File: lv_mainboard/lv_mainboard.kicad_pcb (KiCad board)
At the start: 2 copper layers, 140 x 250 mm, 80 parts, among them J1 Conn_01x02, J10 PWR, J11 Conn_02x05_Counter_Clockwise, J12 Conn_01x04, J13 Conn_02x10_Odd_Even, J14 Conn_01x04, J15 PWR, J16 Conn_01x04, J17 Conn_01x04, J18 Conn_01x02, J19 PWR, J2 Conn_02x10_Odd_Even, J3 Conn_01x03, J4 Conn_01x04, J5 Conn_01x05, J6 Conn_02x10_Odd_Even, J7 Conn_02x10_Odd_Even, J8 Conn_01x04, J9 DE9_Plug_MountingHoles, U1 AP2204K-ADJ, U2 AP2204K-ADJ, U3 AP2204K-ADJ

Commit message: v2025.8
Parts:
- removed C1, C3: 1u, Resistor_SMD:R_0603_1608Metric
- removed C2, C4: 10u, Resistor_SMD:R_0805_2012Metric
- removed C5: 1u, Capacitor_SMD:C_0603_1608Metric_Pad1.08x0.95mm_HandSolder
- removed C6: 10u, Capacitor_SMD:C_0805_2012Metric_Pad1.18x1.45mm_HandSolder
- removed the J12 at (262.0, 311.0)
- removed the J12 at (262.0, 301.5)
- removed the J14 at (280.0, 311.0)
- removed the J14 at (280.0, 301.5)
- removed the J16 at (244.0, 301.5)
- removed the J16 at (244.0, 311.0)
- removed J17: Conn_01x04, Connector_JST:JST_XH_B4B-XH-A_1x04_P2.50mm_Vertical
- removed R3, R5, R7: 100k, Resistor_SMD:R_0603_1608Metric
- removed R4: 301k, Resistor_SMD:R_0603_1608Metric
- removed R6: 165k, Resistor_SMD:R_0603_1608Metric
- removed R8: 866k, Resistor_SMD:R_0603_1608Metric
- removed TP1, TP2, TP3: TestPoint, TestPoint:TestPoint_THTPad_D1.5mm_Drill0.7mm
- removed U1, U2, U3: AP2204K-ADJ, Package_TO_SOT_SMD:SOT-23-5
- removed kibuzzard-682D880A: G***, kibuzzard-682D880A
- removed kibuzzard-682D8819: G***, kibuzzard-682D8819
- removed kibuzzard-682D8830: G***, kibuzzard-682D8830
- removed kibuzzard-682D8907: G***, kibuzzard-682D8907
- removed kibuzzard-682D8919: G***, kibuzzard-682D8919
- removed kibuzzard-682D8927: G***, kibuzzard-682D8927
- removed kibuzzard-682D8AF9: G***, kibuzzard-682D8AF9
- removed kibuzzard-682D8B11: G***, kibuzzard-682D8B11
- removed kibuzzard-682D8B7A: G***, kibuzzard-682D8B7A
- removed kibuzzard-682D8C28: G***, kibuzzard-682D8C28
- removed kibuzzard-682D8E18: G***, kibuzzard-682D8E18
- added J12: Conn_01x04, Connector_JST:JST_XH_B4B-XH-A_1x04_P2.50mm_Vertical, F.Cu at (302.4, 227.4)
- added J14: Conn_01x04, Connector_JST:JST_XH_B4B-XH-A_1x04_P2.50mm_Vertical, F.Cu at (302.3, 244.6)
- added J16: Conn_01x04, Connector_JST:JST_XH_B4B-XH-A_1x04_P2.50mm_Vertical, F.Cu at (302.4, 261.5)
- added J20: Conn_01x02, Connector_JST:JST_XH_B2B-XH-A_1x02_P2.50mm_Vertical, F.Cu at (301.0, 154.5)
- added J21: Conn_01x02, Connector_JST:JST_XH_B2B-XH-A_1x02_P2.50mm_Vertical, F.Cu at (176.0, 202.5)
- added J22: Conn_01x02, Connector_JST:JST_XH_B2B-XH-A_1x02_P2.50mm_Vertical, F.Cu at (290.0, 154.5)
- added J23: Conn_01x03, Connector_JST:JST_XH_B3B-XH-A_1x03_P2.50mm_Vertical, F.Cu at (254.5, 74.5)
- added J24: PWR, Connector_AMASS:AMASS_XT60-M_1x02_P7.20mm_Vertical, F.Cu at (184.5, 89.0)
- added J25: Conn_01x04, Connector_JST:JST_XH_B4B-XH-A_1x04_P2.50mm_Vertical, F.Cu at (291.0, 227.5)
- added J26: Conn_01x04, Connector_JST:JST_XH_B4B-XH-A_1x04_P2.50mm_Vertical, F.Cu at (291.5, 244.7)
- added J27: Conn_01x04, Connector_JST:JST_XH_B4B-XH-A_1x04_P2.50mm_Vertical, F.Cu at (291.5, 261.6)
- J9: value DE9_Plug_MountingHoles -> PWR; footprint Connector_Dsub:DSUB-9_Female_Horizontal_P2.77x2.84mm_EdgePinOffset7.70mm_Housed_MountingHolesOffset9.12mm -> Connector_AMASS:AMASS_XT60-M_1x02_P7.20mm_Vertical
- R1, R2: moved to F.Cu
- moved J18 180.8 mm to (301.0, 167.0), turned to -90 degrees
- moved J4 166.1 mm to (301.5, 180.0)
- moved J8 138.6 mm to (302.0, 210.0)
- moved J9 128.1 mm to (184.6, 100.0), turned to 180 degrees
- moved J1 125.2 mm to (301.5, 196.1)
- moved H21 95.8 mm to (281.4, 168.3)
- moved H22 95.8 mm to (258.4, 168.3)
- moved H23 95.8 mm to (258.4, 211.3)
- moved H24 95.8 mm to (281.4, 211.3)
- moved J2 95.8 mm to (258.2, 201.2)
- moved G*** 75.2 mm to (344.2, 278.5)
- moved G*** 75.2 mm to (344.0, 269.0)
- moved G*** 75.2 mm to (344.0, 253.0)
- moved J5 70.6 mm to (237.5, 74.5), turned to 0 degrees
- moved J13 56.9 mm to (256.7, 126.9)
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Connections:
- J11 pad 3: P4_RGB -> P4_HVbox
- J2 pad 2: SW_signal -> SW_Fault
- J3 pad 2: FAN_PWR -> PUMP_PWR
- J3 pad 3: PUMP_PWR -> FAN_PWR
- J7 pad 11: unconnected-(J7-Pin_11-Pad11) -> GND
- J7 pad 13: unconnected-(J7-Pin_13-Pad13) -> GND
- J7 pad 15: unconnected-(J7-Pin_15-Pad15) -> GND
- J7 pad 17: unconnected-(J7-Pin_17-Pad17) -> GND
- J7 pad 5: unconnected-(J7-Pin_5-Pad5) -> GND
- J7 pad 7: unconnected-(J7-Pin_7-Pad7) -> GND
- J7 pad 9: unconnected-(J7-Pin_9-Pad9) -> GND
- J9 pad 1: BSE_L_init -> P4_HVbox
- J9 pad 2: CAN- -> GND
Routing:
- net GND: track 9.35 -> 416.4 mm, vias 2 -> 825
- net +3V3: track 321.5 -> 0.00 mm, vias 2 -> 0
- net +24V: track 0.00 -> 205.9 mm
- net P5_MCU: track 298.7 -> 109.4 mm
- net P7_ACC: track 340.4 -> 161.8 mm, vias 0 -> 1
- net current_init: track 16.1 -> 124.9 mm, vias 0 -> 2
- net BMS_RST: track 32.9 -> 115.6 mm
- net SW_Fault: track 0.00 -> 82.2 mm, vias 0 -> 1
- net BSPD_LED: track 32.3 -> 107.1 mm
- net BSPD_RST: track 31.2 -> 104.3 mm
- net PUMP_PWR: track 28.7 -> 94.6 mm, vias 0 -> 1
- net SDC_OUT: track 89.1 -> 25.2 mm
- net BMS_LED: track 30.8 -> 94.4 mm
- net FAN_PWR: track 28.7 -> 91.3 mm, vias 0 -> 1
- net P2_BSPD: track 143.2 -> 80.8 mm
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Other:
- board size 140 x 250 mm -> 140 x 220 mm
- board text removed: "GND LED RST VDD"
- board text removed: "GND TASL BMS_F IMD_F"
- board text removed: "GND TASL TSSI 24V"
- board text removed: "GND U1 T1 P1 U2"
- board text removed: "GND pump fan"
- board text removed: "PWM"
- board text removed: "current_in"
- board text removed: "from ACC Box"
- board text removed: "from HV Box"
- board text removed: "to ACC Box"
- board text removed: "to Mainhoop Light"

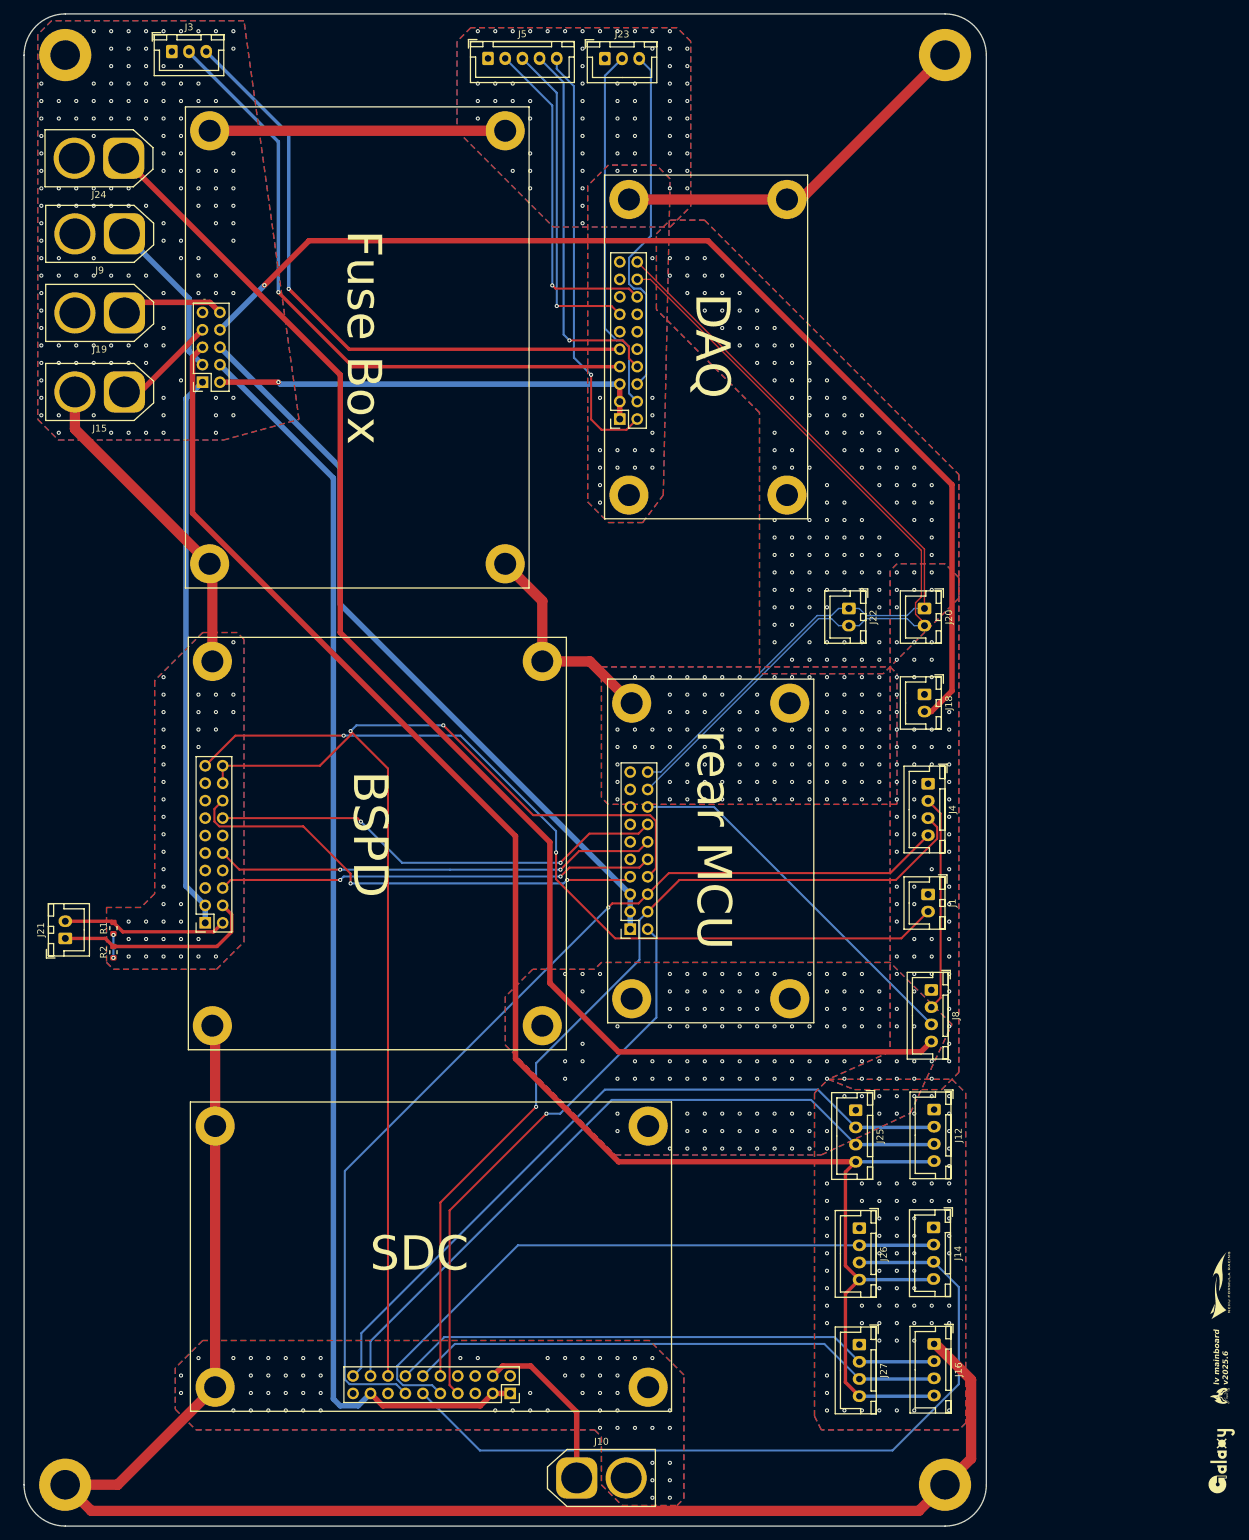
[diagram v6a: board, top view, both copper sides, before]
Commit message: v2025.8 but need to add another DAQ
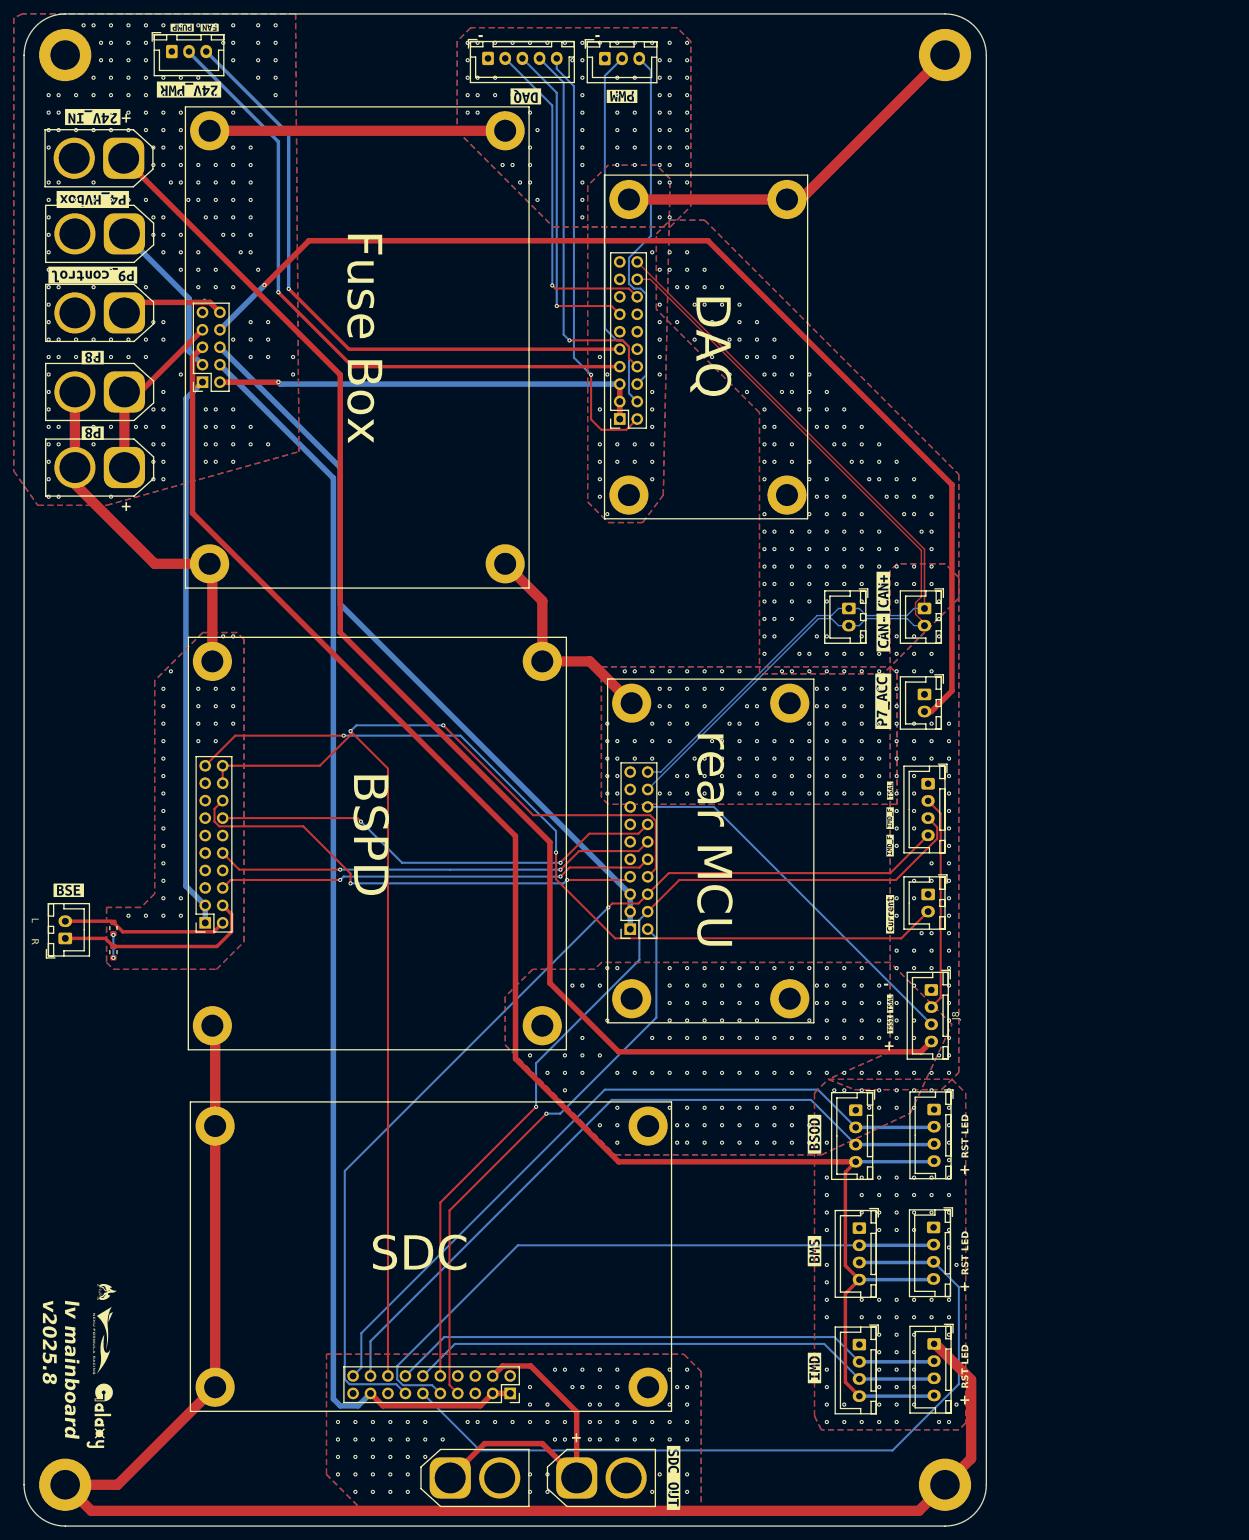
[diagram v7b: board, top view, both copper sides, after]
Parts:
- added J10: PWR, Connector_AMASS:AMASS_XT60-M_1x02_P7.20mm_Vertical, F.Cu at (232.0, 281.0)
- added J15: PWR, Connector_AMASS:AMASS_XT60-M_1x02_P7.20mm_Vertical, F.Cu at (184.6, 134.0)
- added kibuzzard-688F5F64: G***, kibuzzard-688F5F64, F.Cu at (180.0, 83.0)
- added kibuzzard-688F6027: G***, kibuzzard-688F6027, F.Cu at (180.0, 118.0)
- added kibuzzard-688F6027: G***, kibuzzard-688F6027, F.Cu at (180.0, 129.0)
- added kibuzzard-688F6048: G***, kibuzzard-688F6048, F.Cu at (197.0, 70.0)
- added kibuzzard-688F605D: G***, kibuzzard-688F605D, F.Cu at (193.0, 70.0)
- added kibuzzard-688F607C: G***, kibuzzard-688F607C, F.Cu at (194.0, 79.0)
- added kibuzzard-688F632C: G***, kibuzzard-688F632C, F.Cu at (243.0, 80.0)
- added kibuzzard-688F6344: G***, kibuzzard-688F6344, F.Cu at (257.0, 80.0)
- added kibuzzard-688F6381: G***, kibuzzard-688F6381, F.Cu at (295.0, 152.0)
- added kibuzzard-688F638D: G***, kibuzzard-688F638D, F.Cu at (295.0, 158.0)
- added kibuzzard-688F63AA: G***, kibuzzard-688F63AA, F.Cu at (180.0, 95.0)
- added kibuzzard-688F63D0: G***, kibuzzard-688F63D0, F.Cu at (295.0, 168.0)
- added kibuzzard-688F6407: G***, kibuzzard-688F6407, F.Cu at (296.0, 189.0)
- added kibuzzard-688F6412: G***, kibuzzard-688F6412, F.Cu at (296.0, 185.0)
- added kibuzzard-688F6425: G***, kibuzzard-688F6425, F.Cu at (296.0, 181.0)
- added kibuzzard-688F6425: G***, kibuzzard-688F6425, F.Cu at (296.0, 212.0)
- added kibuzzard-688F6442: G***, kibuzzard-688F6442, F.Cu at (296.0, 199.0)
- added kibuzzard-688F6465: G***, kibuzzard-688F6465, F.Cu at (296.0, 215.0)
- added kibuzzard-688F64B0: G***, kibuzzard-688F64B0, F.Cu at (285.0, 265.0)
- added kibuzzard-688F64BC: G***, kibuzzard-688F64BC, F.Cu at (285.0, 248.0)
- added kibuzzard-688F64C5: G***, kibuzzard-688F64C5, F.Cu at (285.0, 231.0)
- added kibuzzard-688F662E: G***, kibuzzard-688F662E, F.Cu at (264.5, 281.0)
- added kibuzzard-688F668F: G***, kibuzzard-688F668F, F.Cu at (176.5, 195.5)
- added kibuzzard-688F6DC2: G***, kibuzzard-688F6DC2, F.Cu at (180.0, 106.0)
- moved G*** 163.4 mm to (181.0, 272.0), turned to -90 degrees
- moved G*** 162.7 mm to (181.5, 261.0), turned to -90 degrees
- moved G*** 162.7 mm to (182.0, 254.0), turned to -90 degrees
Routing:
- net SDC_OUT: track 25.2 -> 47.7 mm
- net P8: track 15.1 -> 26.1 mm
- net GND: track 416.4 -> 421.1 mm, vias 825 -> 981
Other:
- board text added: "+"
- board text added: "L"
- board text added: "LED"
- board text added: "R"
- board text added: "RST"
- board text added: "lv mainboard v2025.8"
- board text removed: "lv mainboard v2025.6"
